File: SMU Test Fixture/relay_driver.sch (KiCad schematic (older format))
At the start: 46 parts, among them U7 ADG1414BRU, U8 ADG1414BRU

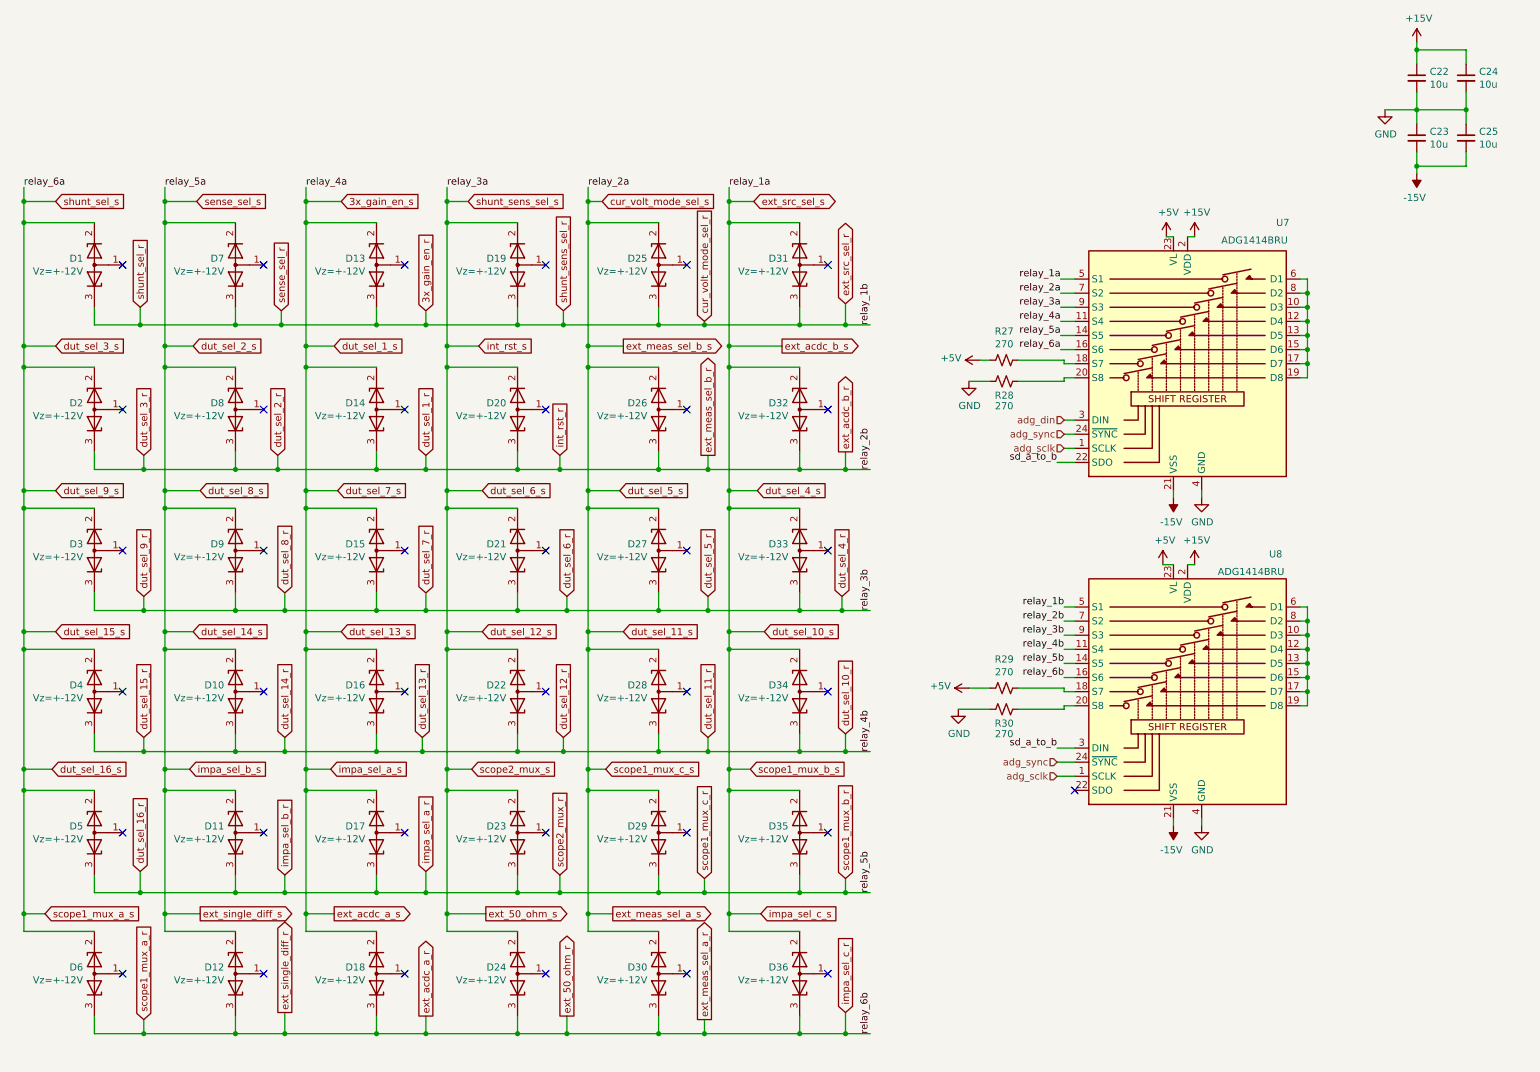
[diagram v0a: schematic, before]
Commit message: Elminate extra scope cal relay, re-organize relays, re-annotate, ERC
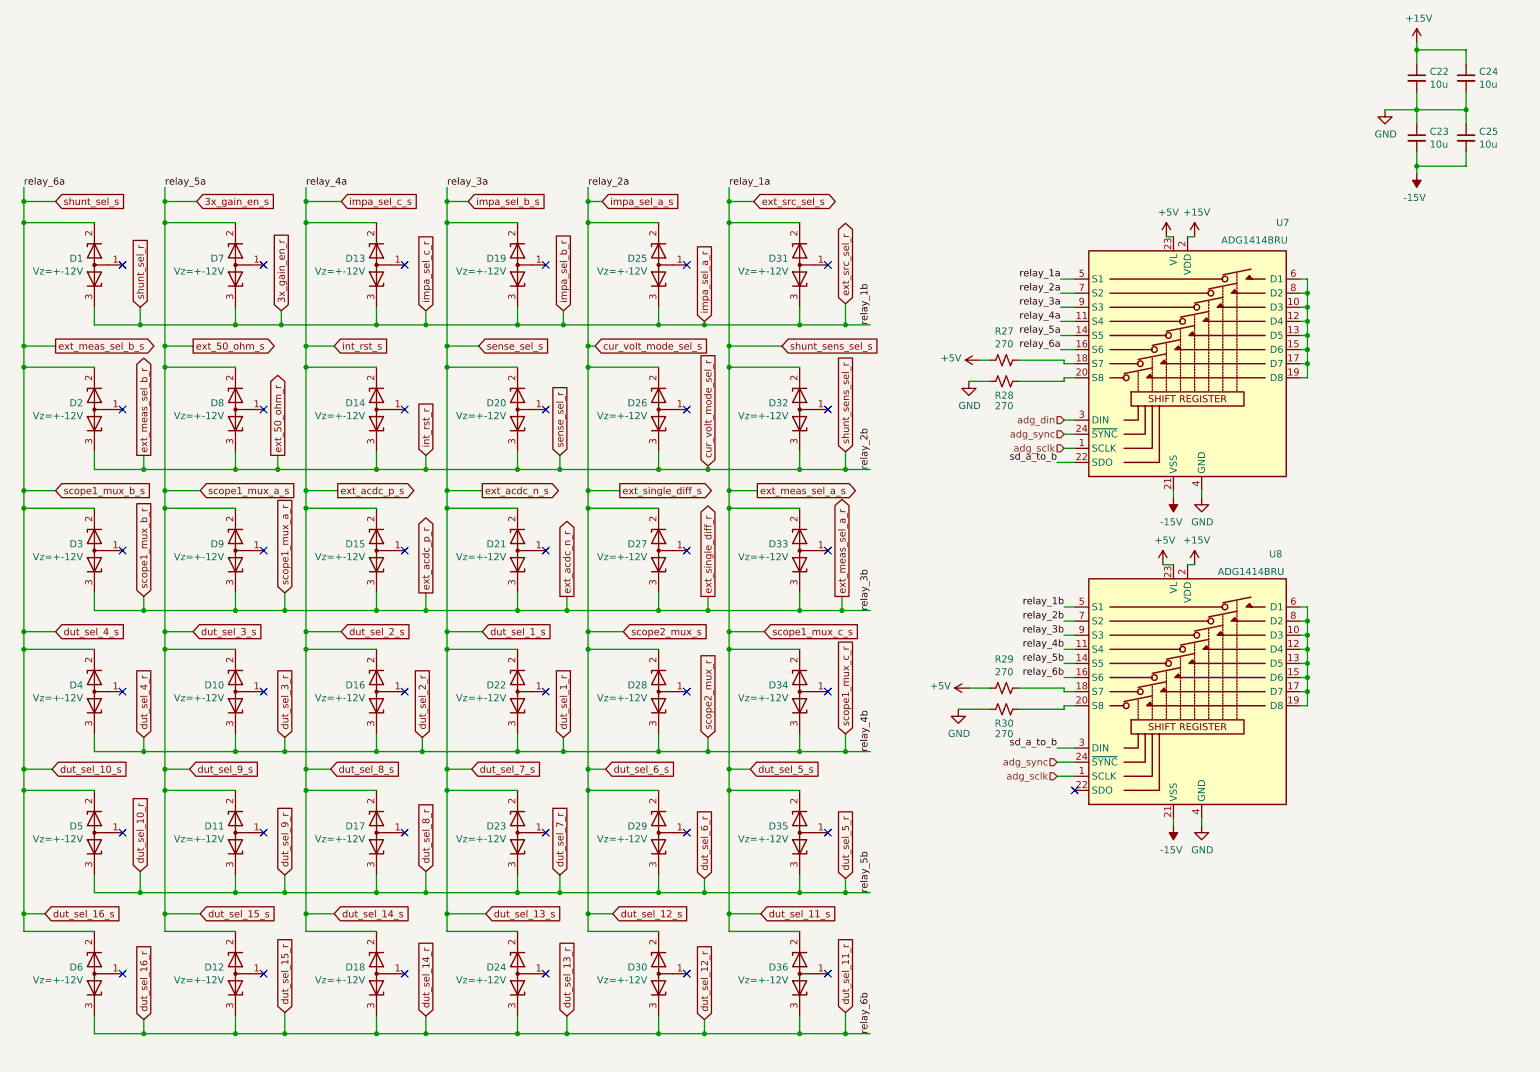
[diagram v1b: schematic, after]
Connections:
- net dut_sel_15_s is gone; now on net dut_sel_10_s: D1.2 (K), D2.2 (K), D3.2 (K), D4.2 (K), D5.2 (K), D6.2 (K), U7.16 (S6)
- net dut_sel_16_r is gone; now on net dut_sel_10_r: D11.3 (K), D17.3 (K), D23.3 (K), D29.3 (K), D35.3 (K), D5.3 (K), U8.14 (S5)
- net 3x_gain_en_s: now also D10.2 (K), D11.2 (K), D12.2 (K), D7.2 (K), D8.2 (K), D9.2 (K), U7.14 (S5); no longer D13.2 (K), D14.2 (K), D15.2 (K), D16.2 (K), D17.2 (K), D18.2 (K), U7.11 (S4)
- net dut_sel_10_r: no longer D10.3 (K), D16.3 (K), D22.3 (K), D28.3 (K), D34.3 (K), D4.3 (K), U8.11 (S4)
- net dut_sel_10_s: no longer D31.2 (K), D32.2 (K), D33.2 (K), D34.2 (K), D35.2 (K), D36.2 (K), U7.5 (S1)
- net dut_sel_14_s: now also D13.2 (K), D14.2 (K), D15.2 (K), D16.2 (K), D17.2 (K), D18.2 (K), U7.11 (S4); no longer D10.2 (K), D11.2 (K), D12.2 (K), D7.2 (K), D8.2 (K), D9.2 (K), U7.14 (S5)
- net dut_sel_1_r: now also D10.3 (K), D16.3 (K), D22.3 (K), D28.3 (K), D34.3 (K), D4.3 (K), U8.11 (S4); no longer D14.3 (K), D2.3 (K), D20.3 (K), D26.3 (K), D32.3 (K), D8.3 (K), U8.7 (S2)
- net dut_sel_12_s renamed dut_sel_13_s
- net dut_sel_4_r renamed ext_acdc_n_r
- net ext_50_ohm_r renamed dut_sel_11_r
- new net cur_volt_mode_sel_r: D14.3 (K), D2.3 (K), D20.3 (K), D26.3 (K), D32.3 (K), D8.3 (K), U8.7 (S2)
- new net dut_sel_11_s: D31.2 (K), D32.2 (K), D33.2 (K), D34.2 (K), D35.2 (K), D36.2 (K), U7.5 (S1)

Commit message: Add footprints for low precision/low power parts.
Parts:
- D1, D10, D11, D12, D13, D14, D15, D16, D17, D18, D19, D2, D20, D21, D22, D23, D24, D25, D26, D27, D28, D29, D3, D30, D31, D32, D33, D34, D35, D36, D4, D5, D6, D7, D8, D9: footprint (none) -> Package_TO_SOT_SMD:SOT-323_SC-70_Handsoldering
- R27, R28, R29, R30: footprint (none) -> Resistor_SMD:R_0805_2012Metric_Pad1.20x1.40mm_HandSolder

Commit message: More footprints added.
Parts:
- C22, C23, C24, C25: footprint (none) -> Capacitor_SMD:C_0805_2012Metric_Pad1.18x1.45mm_HandSolder
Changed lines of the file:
@@
 F 0 "C22" H 10517 996 50  0000 L CNN
 F 1 "10u" H 10517 905 50  0000 L CNN
-F 2 "" H 10425 950 50  0001 C CNN
+F 2 "Capacitor_SMD:C_0805_2012Metric_Pad1.18x1.45mm_HandSolder" H 10425 950 50  0001 C CNN
 F 3 "~" H 10425 950 50  0001 C CNN
 	1    10425 950
@@
 F 0 "C23" H 10517 1421 50  0000 L CNN
 F 1 "10u" H 10517 1330 50  0000 L CNN
-F 2 "" H 10425 1375 50  0001 C CNN
+F 2 "Capacitor_SMD:C_0805_2012Metric_Pad1.18x1.45mm_HandSolder" H 10425 1375 50  0001 C CNN
 F 3 "~" H 10425 1375 50  0001 C CNN
 	1    10425 1375
@@
 F 0 "C24" H 10867 996 50  0000 L CNN
 F 1 "10u" H 10867 905 50  0000 L CNN
-F 2 "" H 10775 950 50  0001 C CNN
+F 2 "Capacitor_SMD:C_0805_2012Metric_Pad1.18x1.45mm_HandSolder" H 10775 950 50  0001 C CNN
 F 3 "~" H 10775 950 50  0001 C CNN
 	1    10775 950
@@
 F 0 "C25" H 10867 1421 50  0000 L CNN
 F 1 "10u" H 10867 1330 50  0000 L CNN
-F 2 "" H 10775 1375 50  0001 C CNN
+F 2 "Capacitor_SMD:C_0805_2012Metric_Pad1.18x1.45mm_HandSolder" H 10775 1375 50  0001 C CNN
 F 3 "~" H 10775 1375 50  0001 C CNN
 	1    10775 1375

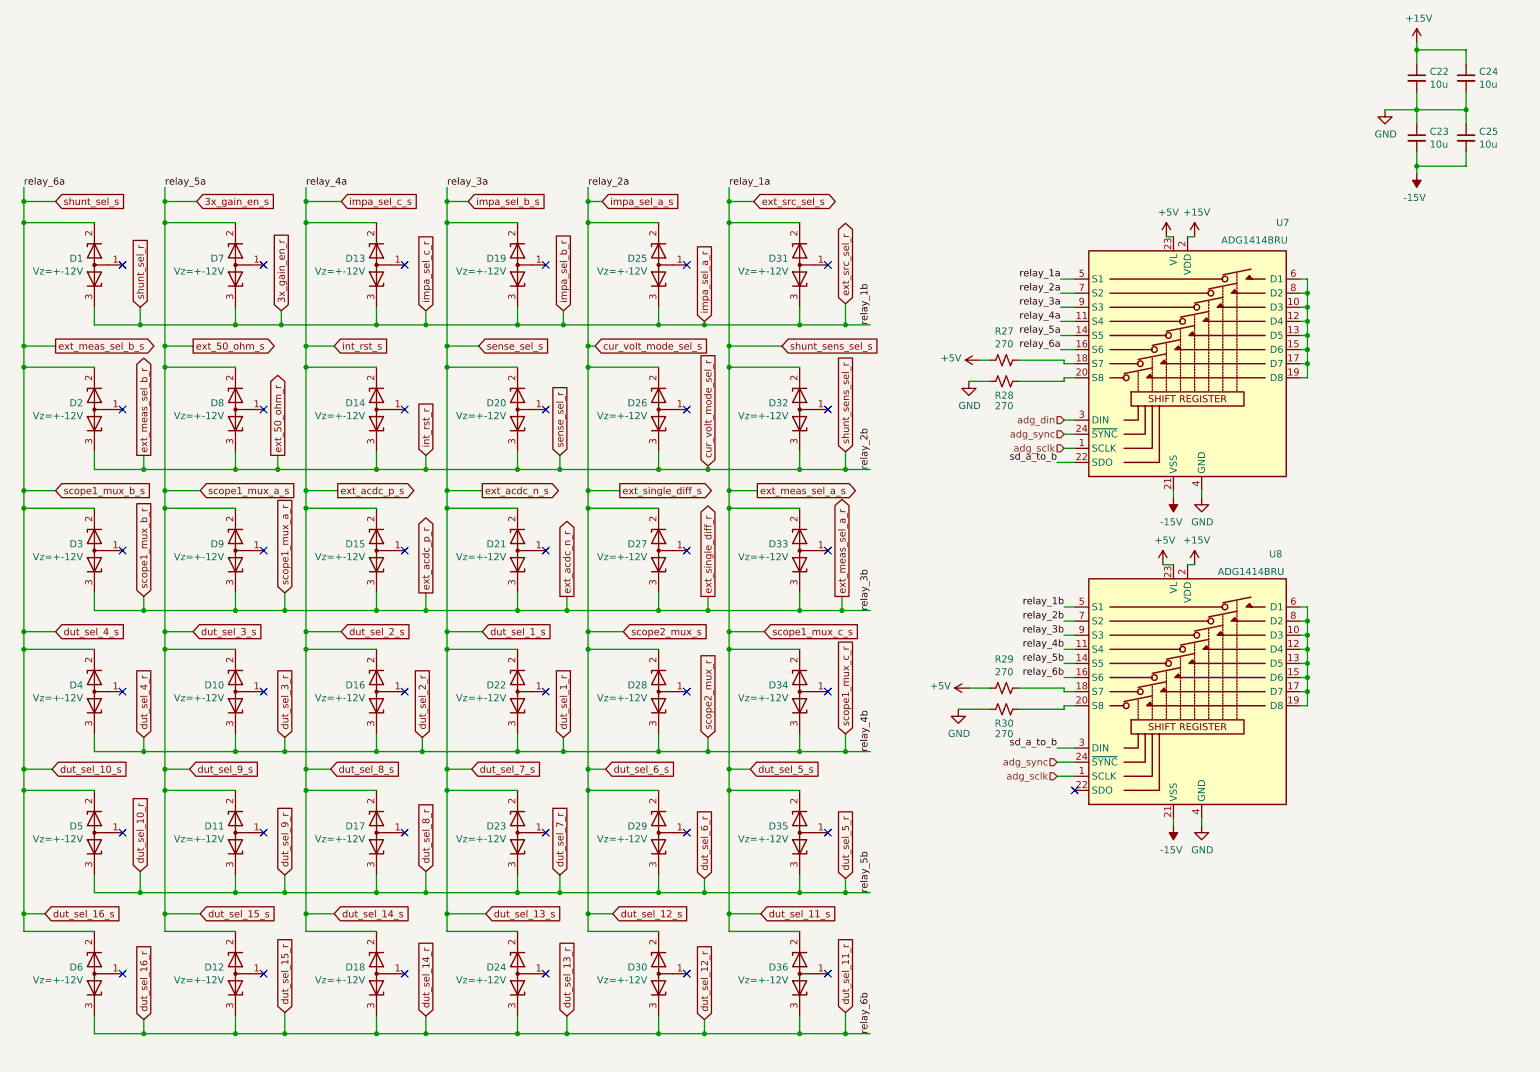
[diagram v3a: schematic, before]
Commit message: Switch to 28V txfrmr, nix preregs, nix 5V for AD2, switch to 12V relay power.
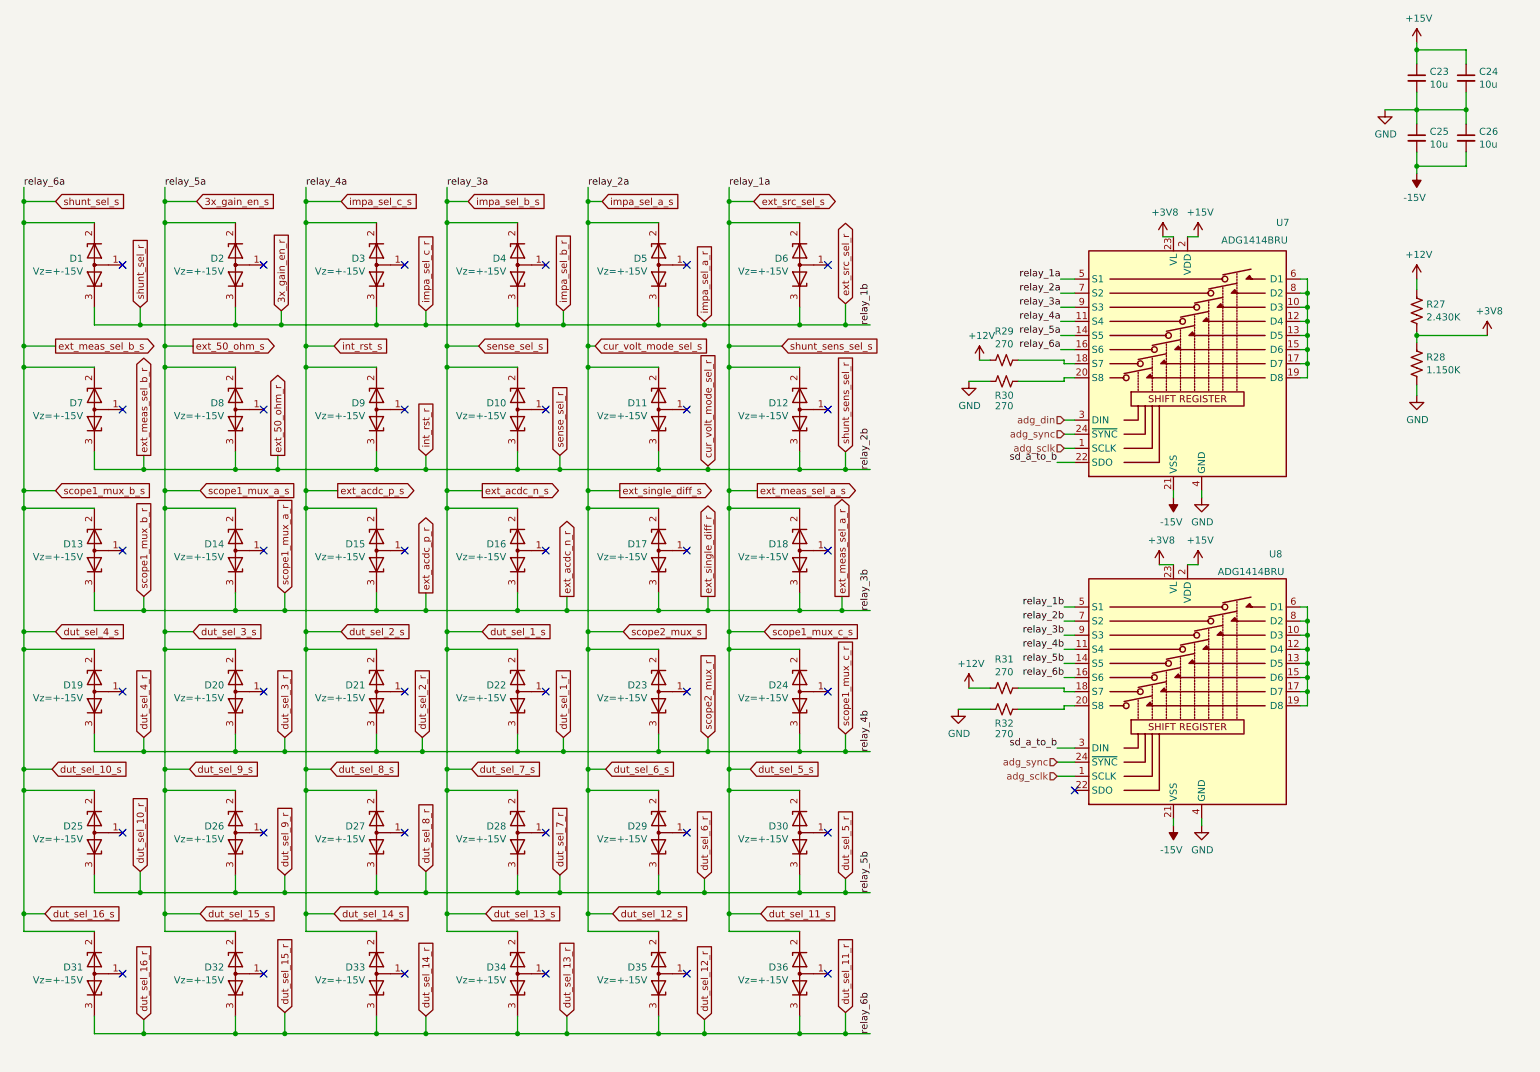
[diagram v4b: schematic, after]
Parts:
- added R27: 2.430K, symbol Device:R_US
- added R28: 1.150K, symbol Device:R_US
- D1, D10, D11, D12, D13, D14, D15, D16, D17, D18, D19, D2, D20, D21, D22, D23, D24, D25, D26, D27, D28, D29, D3, D30, D31, D32, D33, D34, D35, D36, D4, D5, D6, D7, D8, D9: value Vz=+-12V -> Vz=+-15V; PN SZMMBZH12VAWT1G -> MMBZH15VAWT1G
- renumbered C22 to C23, C23 to C25, C25 to C26, R27 to R29, R28 to R30, R29 to R31, R30 to R32
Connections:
- net 3x_gain_en_r: now also D2.3 (K), D3.3 (K), D4.3 (K), D5.3 (K), D6.3 (K); no longer D13.3 (K), D19.3 (K), D25.3 (K), D31.3 (K), D7.3 (K)
- net 3x_gain_en_s: now also D14.2 (K), D2.2 (K), D20.2 (K), D26.2 (K), D32.2 (K); no longer D10.2 (K), D11.2 (K), D12.2 (K), D7.2 (K), D9.2 (K)
- net GND: now also R28.2
- net cur_volt_mode_sel_r: now also D10.3 (K), D11.3 (K), D12.3 (K), D7.3 (K), D9.3 (K); no longer D14.3 (K), D2.3 (K), D20.3 (K), D26.3 (K), D32.3 (K)
- net cur_volt_mode_sel_s: now also D11.2 (K), D17.2 (K), D23.2 (K), D35.2 (K), D5.2 (K); no longer D25.2 (K), D26.2 (K), D27.2 (K), D28.2 (K), D30.2 (K)
- net dut_sel_10_r: now also D25.3 (K), D26.3 (K), D27.3 (K), D28.3 (K), D30.3 (K); no longer D11.3 (K), D17.3 (K), D23.3 (K), D35.3 (K), D5.3 (K)
- net dut_sel_10_s: now also D13.2 (K), D19.2 (K), D25.2 (K), D31.2 (K), D7.2 (K); no longer D2.2 (K), D3.2 (K), D4.2 (K), D5.2 (K), D6.2 (K)
- net dut_sel_11_r: now also D31.3 (K), D32.3 (K), D33.3 (K), D34.3 (K), D35.3 (K); no longer D12.3 (K), D18.3 (K), D24.3 (K), D30.3 (K), D6.3 (K)
- net dut_sel_11_s: now also D12.2 (K), D18.2 (K), D24.2 (K), D30.2 (K), D6.2 (K); no longer D31.2 (K), D32.2 (K), D33.2 (K), D34.2 (K), D35.2 (K)
- net dut_sel_13_s: now also D10.2 (K), D16.2 (K), D28.2 (K), D34.2 (K), D4.2 (K); no longer D19.2 (K), D20.2 (K), D21.2 (K), D23.2 (K), D24.2 (K)
- net dut_sel_14_s: now also D21.2 (K), D27.2 (K), D3.2 (K), D33.2 (K), D9.2 (K); no longer D13.2 (K), D14.2 (K), D16.2 (K), D17.2 (K), D18.2 (K)
- net dut_sel_1_r: now also D19.3 (K), D20.3 (K), D21.3 (K), D23.3 (K), D24.3 (K); no longer D10.3 (K), D16.3 (K), D28.3 (K), D34.3 (K), D4.3 (K)
- net ext_acdc_n_r: now also D13.3 (K), D14.3 (K), D16.3 (K), D17.3 (K), D18.3 (K); no longer D21.3 (K), D27.3 (K), D3.3 (K), D33.3 (K), D9.3 (K)
- net +5V renamed +12V
- net +12V: now also R27.1; no longer U7.23 (VL), U8.23 (VL)
- new net +3V8: R27.2, R28.1, U7.23 (VL), U8.23 (VL)
